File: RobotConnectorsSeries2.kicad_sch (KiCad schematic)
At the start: 21 parts, among them U49 LM2903DR, U50 LM2903DR

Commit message: Change USS plugs and level shifter
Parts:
- R41, R42: footprint Resistor_SMD:R_0603_1608Metric_Pad0.98x0.95mm_HandSolder -> Resistor_SMD:R_0603_1608Metric
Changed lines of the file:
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@@
 		(title "OpenMower SABO Carrierboard for Series I & II")
 		(date "2026-05-26")
-		(rev "v0.5")
+		(rev "v0.6")
 		(company "Apeheanger <joerg@ebeling.ws> for OpenMower")
 		(comment 1 "This design is licensed under CC BY-NC 4.0")
@@
 	(wire
 		(pts
+			(xy 21.59 19.05) (xy 43.18 19.05)
+		)
+		(stroke
+			(width 0)
+			(type default)
+		)
+	)
+	(wire
+		(pts
 			(xy 72.39 156.21) (xy 72.39 162.56)
 		)
@@
 	(wire
 		(pts
-			(xy 21.59 19.05) (xy 43.18 19.05)
-		)
-		(stroke
-			(width 0)
-			(type default)
-		)
-	)
-	(wire
-		(pts
 			(xy 85.09 48.26) (xy 105.41 48.26)
 		)
@@
 		)
 	)
+	(label "5V"
+		(at 43.18 19.05 0)
+		(effects
+			(font
+				(size 1.27 1.27)
+			)
+			(justify left bottom)
+		)
+	)
 	(label "MC_PHASE.V"
 		(at 91.44 48.26 0)
@@
 		)
 	)
-	(label "5V"
-		(at 43.18 19.05 0)
-		(effects
-			(font
-				(size 1.27 1.27)
-			)
-			(justify left bottom)
-		)
-	)
 	(label "MR_HALL_SENSOR.U"
 		(at 101.6 123.19 0)
@@
 		)
 	)
-	(hierarchical_label "5V"
-		(shape input)
-		(at 21.59 19.05 180)
+	(hierarchical_label "HALL0_5V"
+		(shape output)
+		(at 149.86 130.81 180)
 		(effects
 			(font
@@
 		)
 	)
+	(hierarchical_label "HALL3_5V"
+		(shape output)
+		(at 100.33 153.67 0)
+		(effects
+			(font
+				(size 1.27 1.27)
+			)
+			(justify left)
+		)
+	)
 	(hierarchical_label "LCD_~{C}D_3V"
 		(shape input)
@@
 		)
 	)
+	(hierarchical_label "LCD_BACKLIGHT_ANODE"
+		(shape input)
+		(at 209.55 57.15 0)
+		(effects
+			(font
+				(size 1.27 1.27)
+			)
+			(justify left)
+		)
+	)
 	(hierarchical_label "SPI_MISO_5V"
 		(shape output)
@@
 		)
 	)
-	(hierarchical_label "LCD_BACKLIGHT_ANODE"
-		(shape input)
-		(at 209.55 57.15 0)
-		(effects
-			(font
-				(size 1.27 1.27)
-			)
-			(justify left)
-		)
-	)
 	(hierarchical_label "LCD_CLK_3V"
 		(shape input)
@@
 		)
 	)
-	(hierarchical_label "HALL1_5V"
-		(shape output)
-		(at 266.7 130.81 0)
-		(effects
-			(font
-				(size 1.27 1.27)
-			)
-			(justify left)
-		)
-	)
 	(hierarchical_label "MR_PHASE{U V W}"
 		(shape input)
@@
 		)
 	)
+	(hierarchical_label "HALL1_5V"
+		(shape output)
+		(at 266.7 130.81 0)
+		(effects
+			(font
+				(size 1.27 1.27)
+			)
+			(justify left)
+		)
+	)
 	(hierarchical_label "BMS_I2C_SDA"
 		(shape output)
@@
 		)
 	)
-	(hierarchical_label "HALL2_5V"
-		(shape output)
-		(at 274.32 44.45 0)
+	(hierarchical_label "LCD_BACKLIGHT_KATHODE"
+		(shape input)
+		(at 185.42 66.04 180)
 		(effects
 			(font
 				(size 1.27 1.27)
 			)
-			(justify left)
+			(justify right)
 		)
 	)
@@
 		)
 	)
-	(hierarchical_label "HALL3_5V"
+	(hierarchical_label "HALL2_5V"
 		(shape output)
-		(at 100.33 153.67 0)
+		(at 274.32 44.45 0)
 		(effects
 			(font
@@
 		)
 	)
-	(hierarchical_label "BTN_SH{slash}~{LD}_5V"
+	(hierarchical_label "5V"
 		(shape input)
-		(at 180.34 36.83 180)
+		(at 21.59 19.05 180)
 		(effects
 			(font
@@
 		)
 	)
-	(hierarchical_label "LCD_~{CE}_3V"
+	(hierarchical_label "BTN_SH{slash}~{LD}_5V"
 		(shape input)
-		(at 209.55 59.69 0)
+		(at 180.34 36.83 180)
 		(effects
 			(font
 				(size 1.27 1.27)
 			)
-			(justify left)
+			(justify right)
 		)
 	)
-	(hierarchical_label "HALL0_5V"
-		(shape output)
-		(at 149.86 130.81 180)
+	(hierarchical_label "LCD_~{CE}_3V"
+		(shape input)
+		(at 209.55 59.69 0)
 		(effects
 			(font
 				(size 1.27 1.27)
 			)
-			(justify right)
+			(justify left)
 		)
 	)
@@
 		)
 	)
-	(hierarchical_label "LCD_BACKLIGHT_KATHODE"
-		(shape input)
-		(at 185.42 66.04 180)
-		(effects
-			(font
-				(size 1.27 1.27)
-			)
-			(justify right)
-		)
-	)
 	(hierarchical_label "SPI_MOSI_5V"
 		(shape input)
@@
 			)
 		)
-		(property "Footprint" "Resistor_SMD:R_0603_1608Metric_Pad0.98x0.95mm_HandSolder"
+		(property "Footprint" "Resistor_SMD:R_0603_1608Metric"
 			(at 258.318 54.61 90)
 			(hide yes)
@@
 			)
 		)
-		(property "Footprint" "Resistor_SMD:R_0603_1608Metric_Pad0.98x0.95mm_HandSolder"
+		(property "Footprint" "Resistor_SMD:R_0603_1608Metric"
 			(at 224.028 106.68 90)
 			(hide yes)

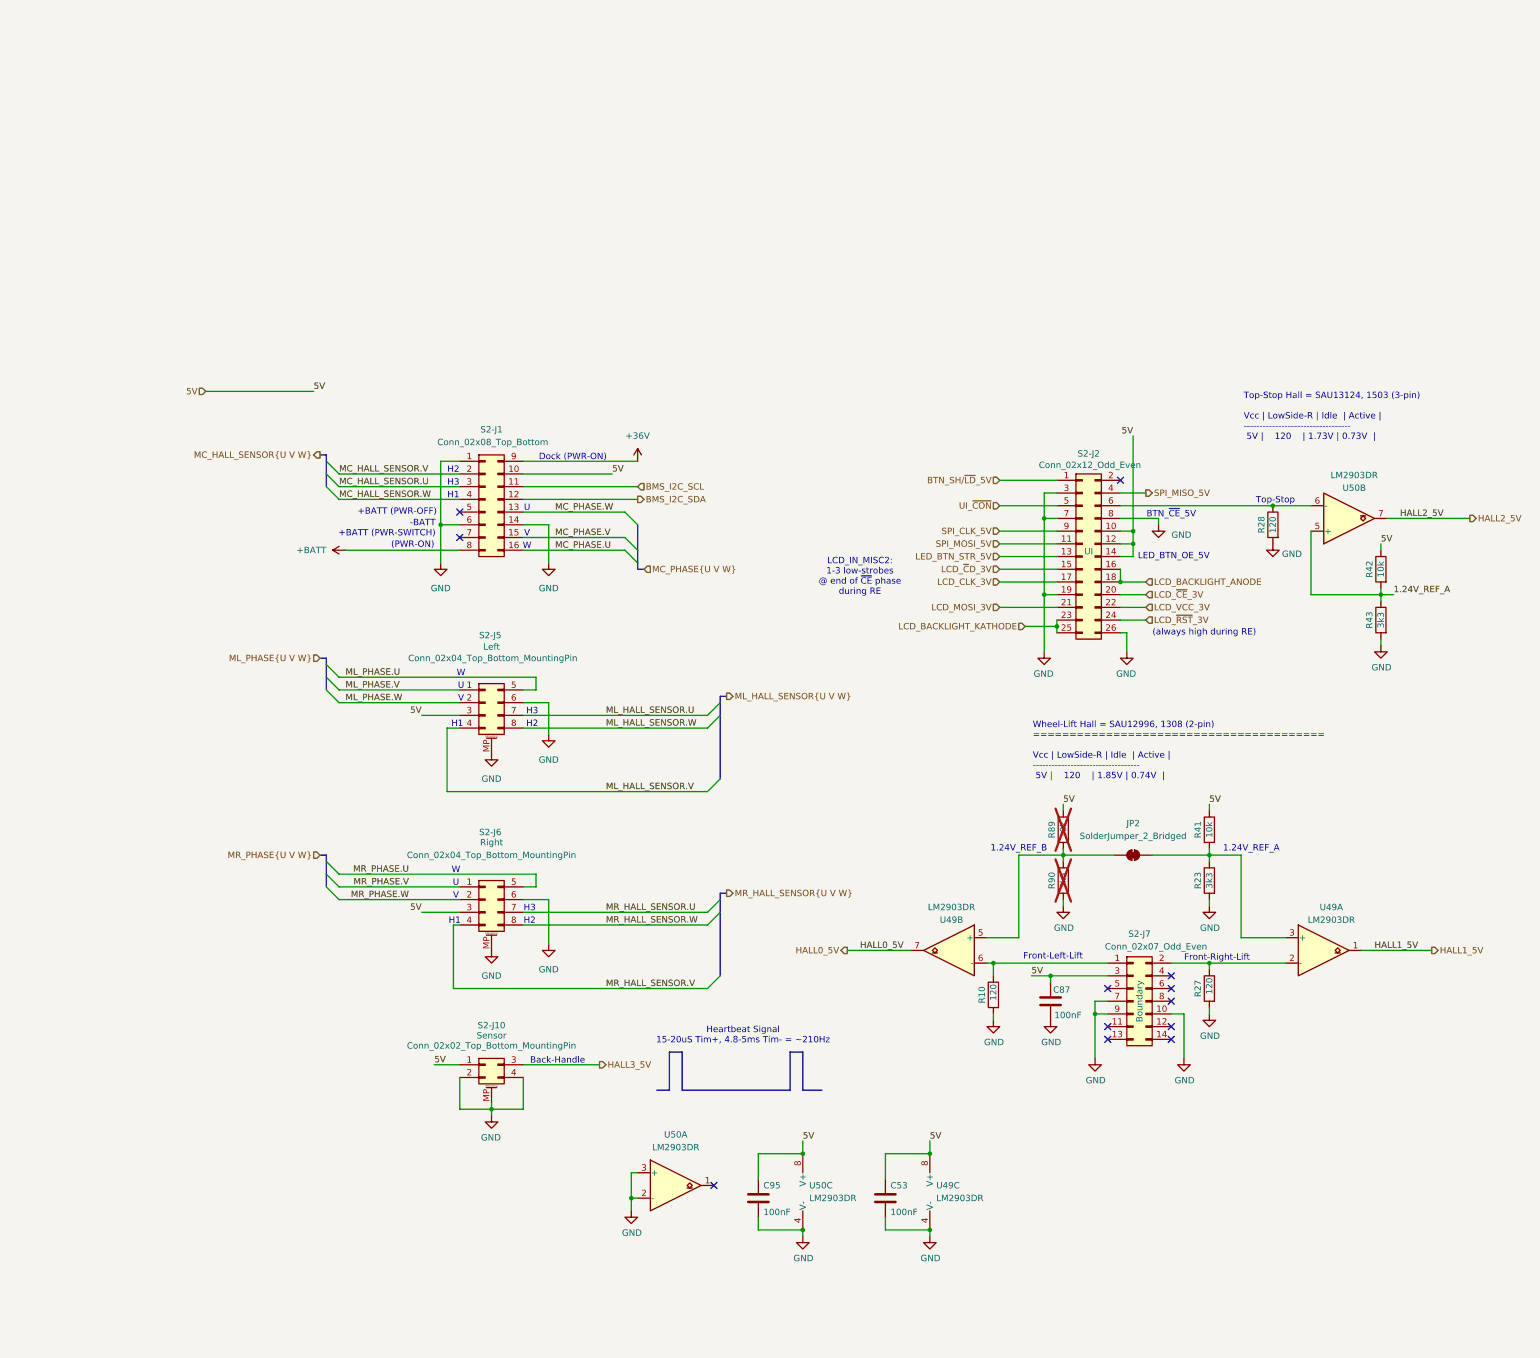
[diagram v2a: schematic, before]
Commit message: Add Series Variants and do some final optimizations
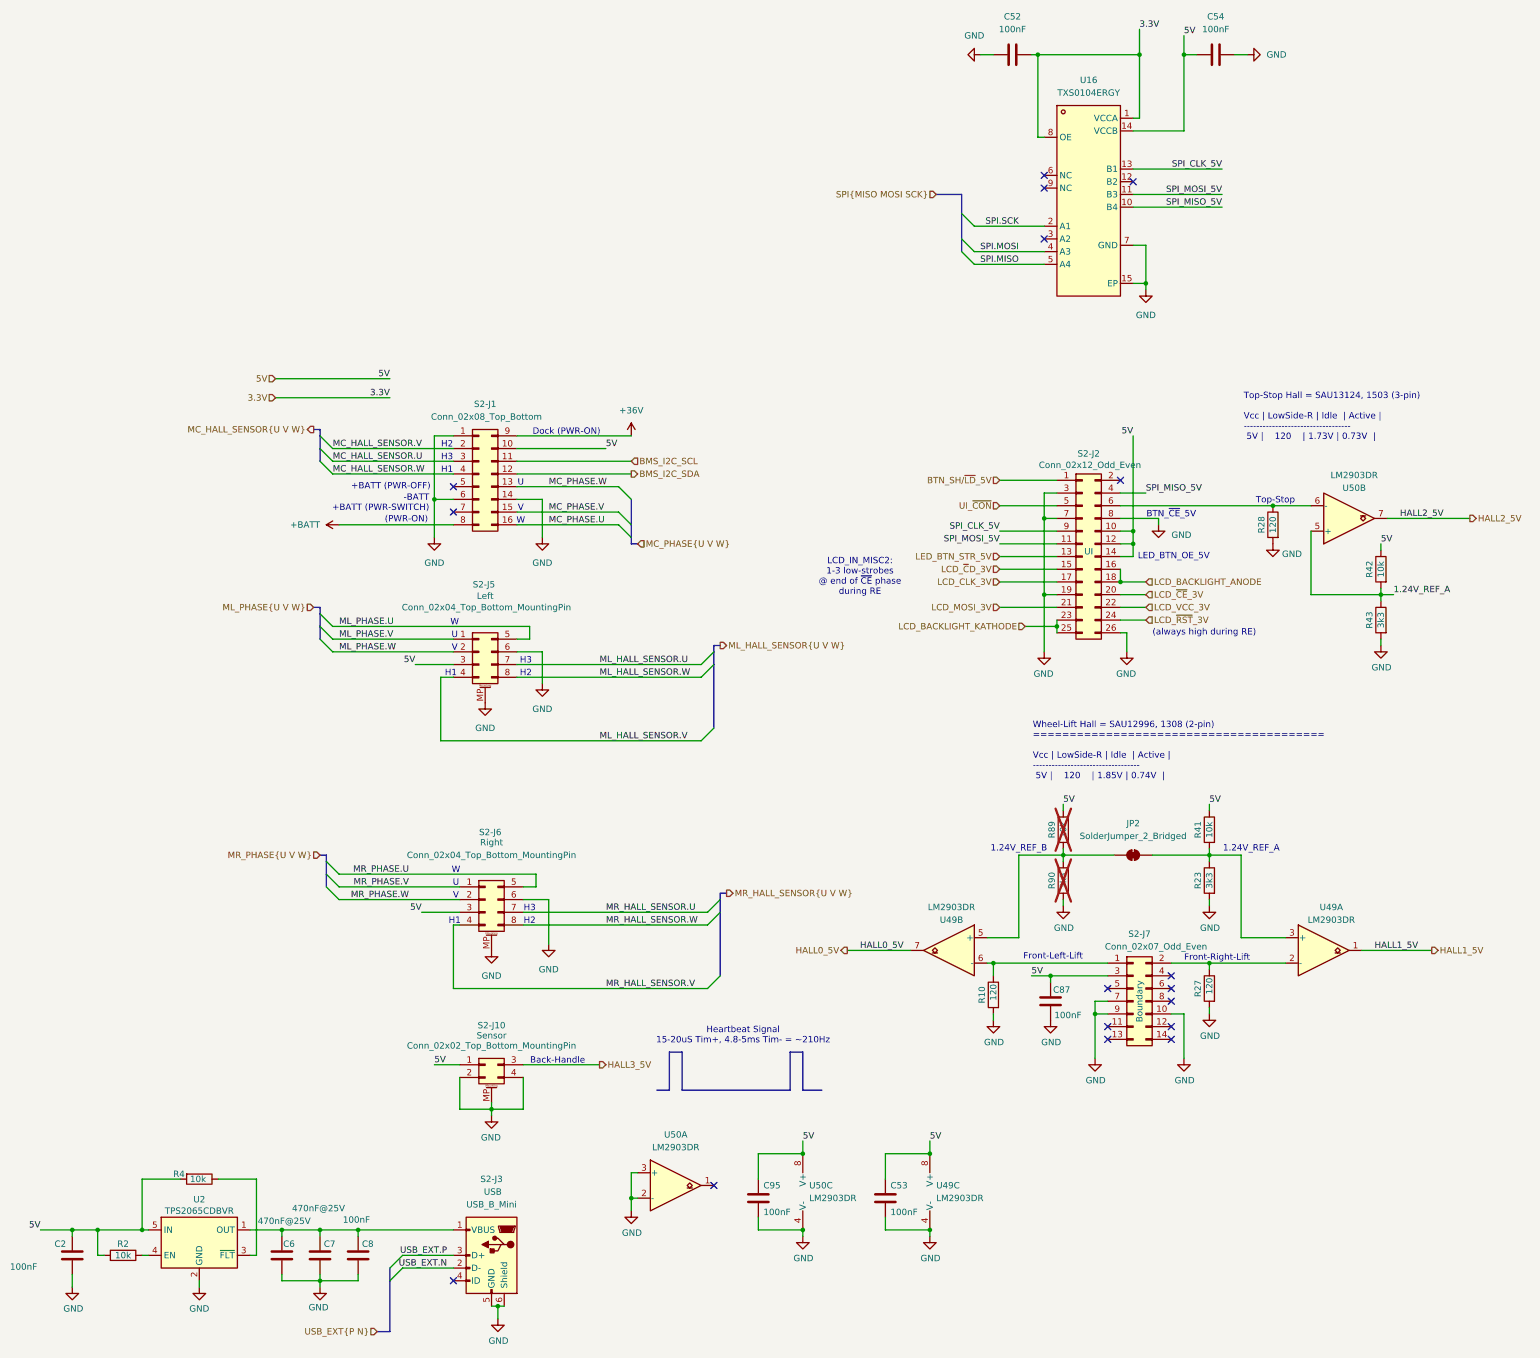
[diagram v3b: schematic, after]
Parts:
- added C2, C52, C54, C8: 100nF, Capacitor_SMD:C_0402_1005Metric, symbol Device:C
- added C6, C7: 470nF@25V, Capacitor_SMD:C_0603_1608Metric, symbol Device:C
- added R2, R4: 10k, Resistor_SMD:R_0402_1005Metric, symbol Device:R
- added S2-J3: USB_B_Mini, easyeda2kicad:MINI-USB-TH_C13453, symbol Connector:USB_B_Mini
- added U16: TXS0104ERGY, nlbn:TXS0104ERGY_C48940325, symbol nlbn:TXS0104ERGY_C48940325
- added U2: TPS2065CDBVR, Package_TO_SOT_SMD:SOT-23-5, symbol Power_Management:TPS2065CDBV
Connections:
- net 5V: now also C2.1, C54.1, R2.2, R4.2, U16.14 (VCCB), U2.5 (IN)
- net GND: now also C2.2, C52.1, C54.2, C6.1, C7.1, C8.2, S2-J3.5 (GND), S2-J3.6 (Shield), U16.15 (EP), U16.7 (GND), U2.2 (GND)
- net SPI_CLK_5V: now also U16.13 (B1)
- net SPI_MISO_5V: now also U16.10 (B4)
- net SPI_MOSI_5V: now also U16.11 (B3)
- new net: C6.2, C7.2, C8.1, S2-J3.1 (VBUS), U2.1 (OUT)
- new net: R4.1, U2.3 (~{FLT})
- new net: R2.1, U2.4 (EN)
- new net 3.3V: C52.2, U16.1 (VCCA), U16.8 (OE)
- new net SPI.MISO: U16.5 (A4)
- new net SPI.MOSI: U16.4 (A3)
- new net SPI.SCK: U16.2 (A1)
- new net USB_EXT.N: S2-J3.2 (D-)
- new net USB_EXT.P: S2-J3.3 (D+)
- no-connect marks 12 -> 17
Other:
- moved on the sheet: S2-J1, S2-J5
